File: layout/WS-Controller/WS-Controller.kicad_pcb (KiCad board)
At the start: 2 copper layers, 76.2 x 83.8 mm, 41 parts, among them J2 Conn_01x06, J4 Conn_01x06, J6 Conn_01x15, J7 Conn_01x15, J8 Conn_01x04, J9 Conn_01x04, K1 G5V-2, K2 G5V-2, M2 Jumper, Q1 BC547, Q2 BC547

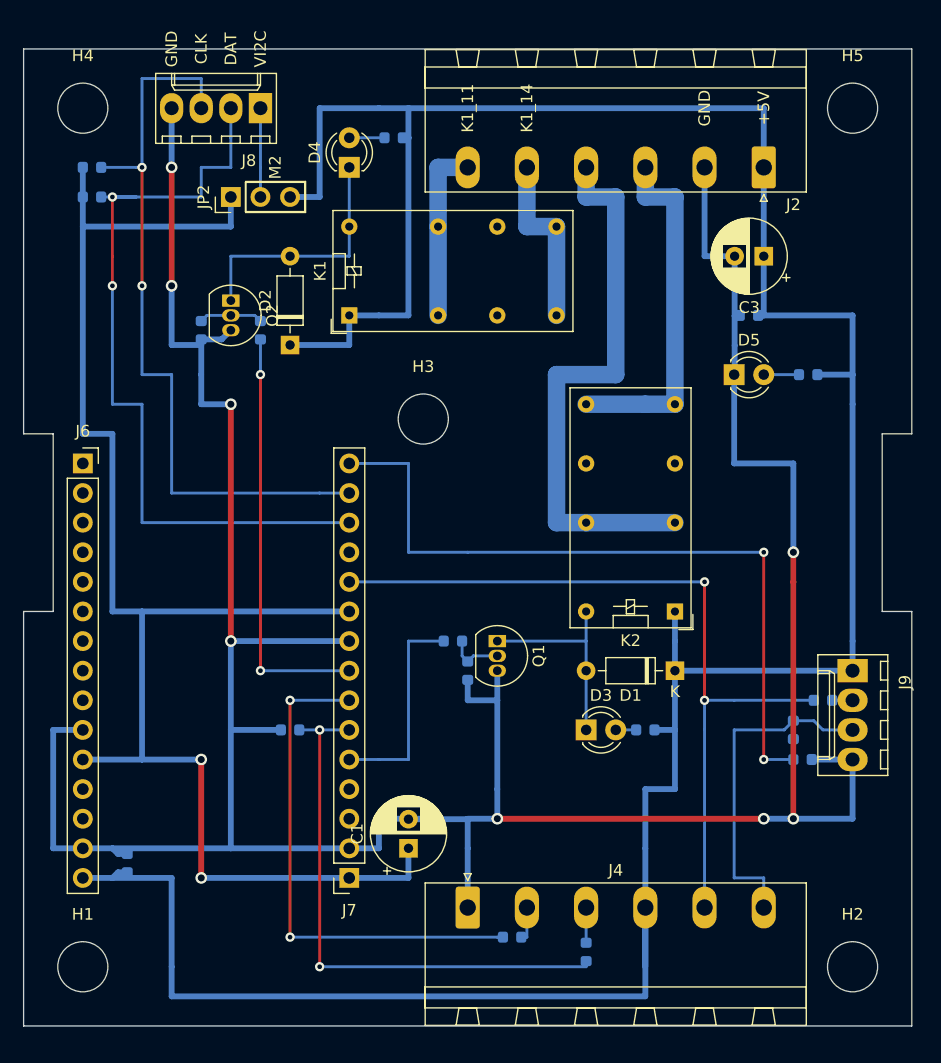
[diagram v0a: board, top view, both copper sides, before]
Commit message: Schaltplan für Wemos-D1
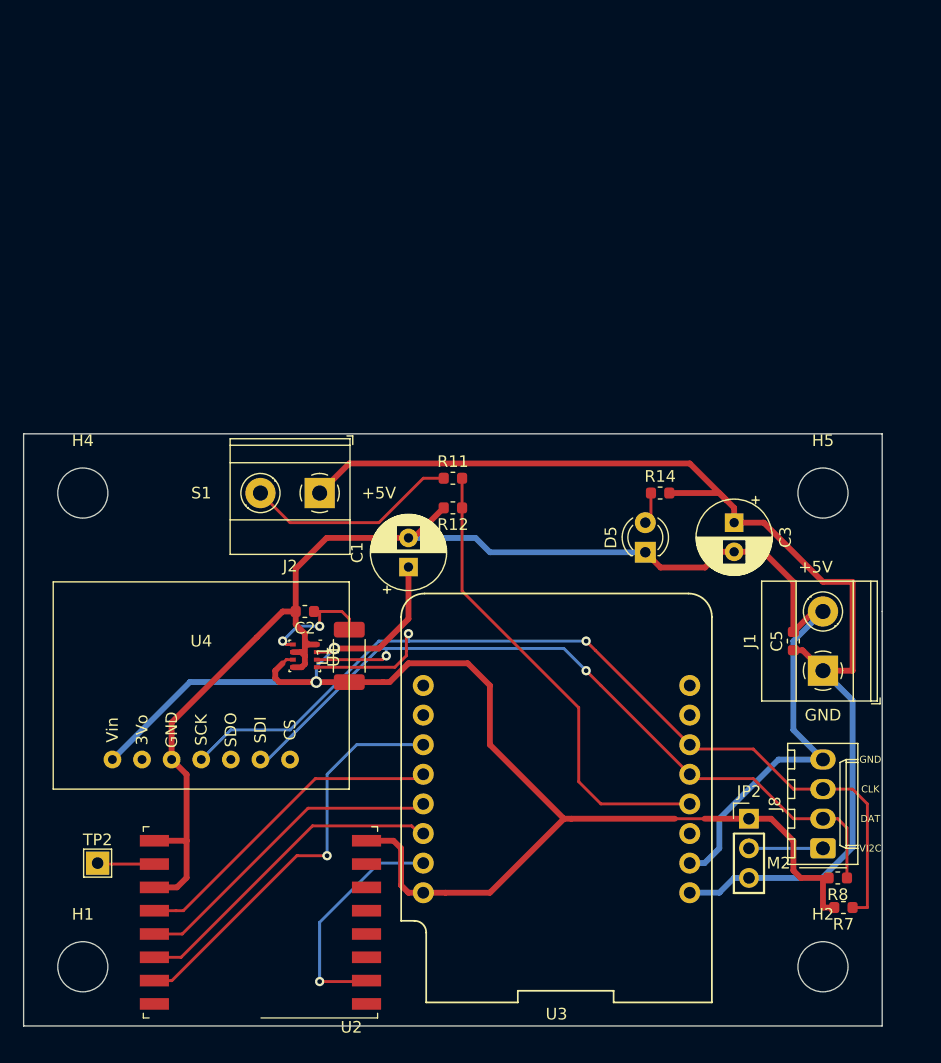
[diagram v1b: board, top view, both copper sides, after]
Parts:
- removed D1, D2: 1N4148, Diode_THT:D_DO-35_SOD27_P7.62mm_Horizontal
- removed D3, D4: LED_Small, LED_THT:LED_D3.0mm
- removed H3: MountingHole, MountingHole:MountingHole_4.3mm_M4_ISO14580
- removed J4: Conn_01x06, Connector_Phoenix_MSTB:PhoenixContact_MSTBA_2,5_6-G-5,08_1x06_P5.08mm_Horizontal
- removed J6, J7: Conn_01x15, Connector_PinSocket_2.54mm:PinSocket_1x15_P2.54mm_Vertical
- removed J9: Conn_01x04, kp_Connectors_Wuerth:WR-WTB-04-V
- removed K1, K2: G5V-2, Relay_THT:Relay_DPDT_Omron_G5V-2
- removed Q1, Q2: BC547, Package_TO_SOT_THT:TO-92_Inline
- removed R1, R3: 330, Resistor_SMD:R_0603_1608Metric
- removed R10, R2: 1K5, Resistor_SMD:R_0603_1608Metric
- removed R16: 2K2, Resistor_SMD:R_0603_1608Metric
- removed R17: 1K2, Resistor_SMD:R_0603_1608Metric
- removed R4, R5: 100K, Resistor_SMD:R_0603_1608Metric
- removed R6, R9: 4R7, Resistor_SMD:R_0603_1608Metric
- added J1: Conn_01x02, TerminalBlock_Phoenix:TerminalBlock_Phoenix_MKDS-1,5-2-5.08_1x02_P5.08mm_Horizontal, F.Cu at (157.5, 129.5)
- added L1: L, Inductor_SMD:L_2010_5025Metric, F.Cu at (116.8, 128.3)
- added TP2: TestPoint, TestPoint:TestPoint_THTPad_2.0x2.0mm_Drill1.0mm, F.Cu at (95.2, 146.1)
- added U1: BME280, Package_LGA:Bosch_LGA-8_2.5x2.5mm_P0.65mm_ClockwisePinNumbering, F.Cu at (113.0, 128.3)
- added U2: RFM69W, RF_Module:HOPERF_RFM69HW, F.Cu at (109.2, 151.1)
- added U3: WeMos_D1_mini, Zielke:wemos-d1-mini, F.Cu at (134.6, 139.7)
- added U4: Adafruit_BME280, Zielke:ADAFRUIT_BME280, F.Cu at (104.1, 137.2)
- C2, C5, R11, R12, R14, R7, R8: moved to F.Cu
- J2: value Conn_01x06 -> Conn_01x02; footprint Connector_Phoenix_MSTB:PhoenixContact_MSTBA_2,5_6-G-5,08_1x06_P5.08mm_Horizontal -> TerminalBlock_Phoenix:TerminalBlock_Phoenix_MKDS-1,5-2-5.08_1x02_P5.08mm_Horizontal
- J8: footprint kp_Connectors_Wuerth:WR-WTB-04-V -> Connector_Molex:Molex_KK-254_AE-6410-04A_1x04_P2.54mm_Vertical
- moved R7 90.5 mm to (159.2, 149.9)
- moved R8 86.6 mm to (158.8, 147.3)
- moved J8 79.8 mm to (157.5, 144.8), turned to 90 degrees
- moved M2 70.1 mm to (151.1, 146.1), turned to 0 degrees
- moved JP2 69.4 mm to (151.1, 142.2), turned to 0 degrees
- moved J2 47.2 mm to (114.3, 114.3)
- moved R11 42.2 mm to (125.7, 113.0), turned to 0 degrees
- moved H5 33.1 mm to (157.5, 114.3)
- moved H4 33.0 mm to (94.0, 114.3)
- moved C5 28.2 mm to (154.9, 127.0), turned to 90 degrees
- moved C2 26.4 mm to (113.0, 124.5), turned to 180 degrees
- moved C1 24.1 mm to (121.9, 120.7)
- moved R12 23.6 mm to (125.7, 115.6)
- moved C3 23.0 mm to (149.9, 116.8), turned to 270 degrees
- moved D5 17.0 mm to (142.2, 119.4), turned to 90 degrees
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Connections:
- net /GPIO13 renamed /D3
- net /GPIO4_DAT renamed /SDA
- net /GPIO5_CLK renamed /SCL
- C2 pad 1: +5V -> Net-(C2-Pad1)
- J2 pad 2: GND -> /SW_Reserved
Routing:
- net +5V: track 256.1 -> 102.1 mm
- net GND: track 273.9 -> 135.8 mm, vias 8 -> 0
- net /GPIO2: track 67.8 -> 0.00 mm, vias 2 -> 0
- net /GPIO16: track 65.3 -> 0.00 mm, vias 2 -> 0
- net /K2-11: track 48.3 -> 0.00 mm
- net /GPIO12: track 43.7 -> 0.00 mm, vias 2 -> 0
- net /GPIO14: track 36.0 -> 0.00 mm, vias 2 -> 0
- net /SS: track 0.00 -> 35.6 mm, vias 0 -> 1
- net /K2-14: track 30.5 -> 0.00 mm
- net /Echo: track 28.6 -> 0.00 mm
- net /MOSI: track 0.00 -> 28.2 mm
- net /SCK: track 0.00 -> 27.8 mm
- net /MISO: track 0.00 -> 27.6 mm
- net /SCL: track 64.5 -> 87.8 mm
- net Net-(D2-Pad2): track 21.6 -> 0.00 mm
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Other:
- board size 76.2 x 83.8 mm -> 73.7 x 50.8 mm
- board text added: "S1"
- board text removed: "K1_11"
- board text removed: "K1_14"
